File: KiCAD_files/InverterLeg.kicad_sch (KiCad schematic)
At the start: 94 parts, among them J801 Conn_Coaxial_Small, J802 Conn_Coaxial_Small, J804 Conn_01x03_Socket, J811 Screw_Terminal_01x01, J814 Screw_Terminal_01x01, J817 Screw_Terminal_01x01, J825 HC-PBB08-2-08-M-H4.0-G1-R-P-04, J827 HC-PBB08-2-08-M-H4.0-G1-R-P-04, J831 HC-PBB08-2-08-M-H4.0-G1-R-P-04, T801 TE1212-2W6ENT, T802 TE1212-2W6ENT, U603 UCC21520, U704 VPS8701B, U707 VPS8701B, U801 LT1761-SD, U802 LT1761-SD, U811 TMP117xxDRV, U815 TMP117xxDRV

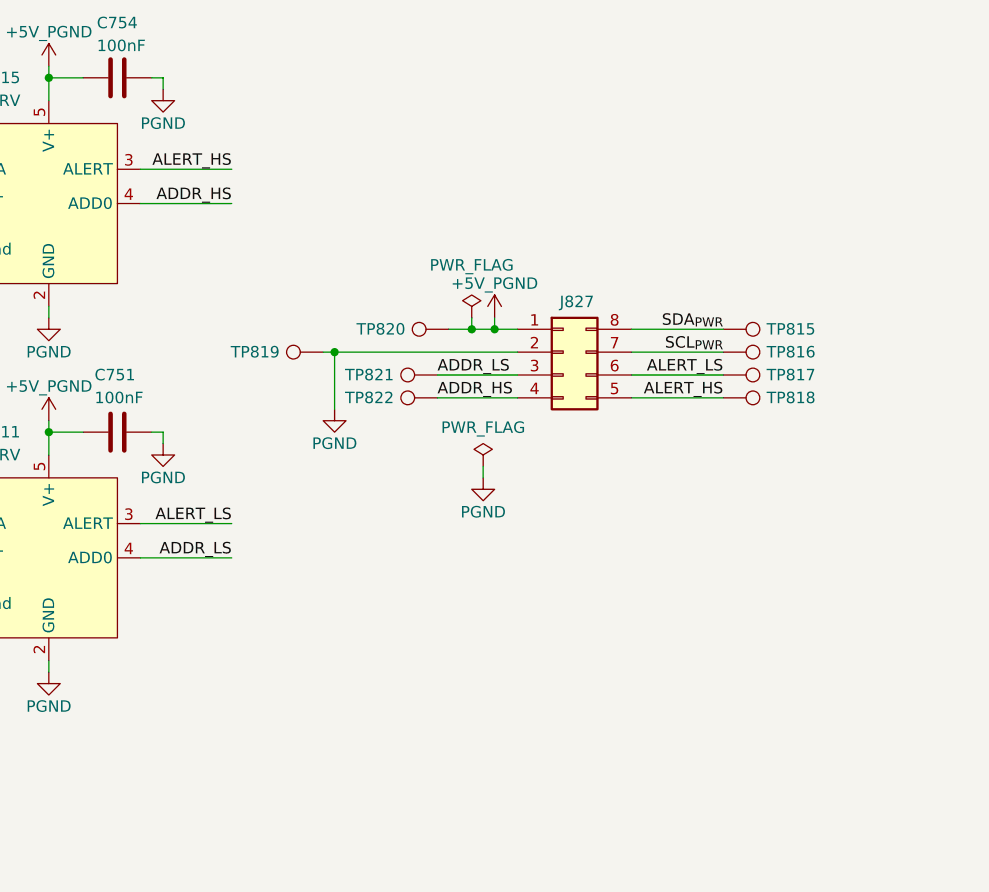
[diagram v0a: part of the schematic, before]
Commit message: Added an EEPROM footprint. Mooved slightly thermal sensor connector.
Signed-off-by: Jean Alinei <jean.alinei@owntech.org>
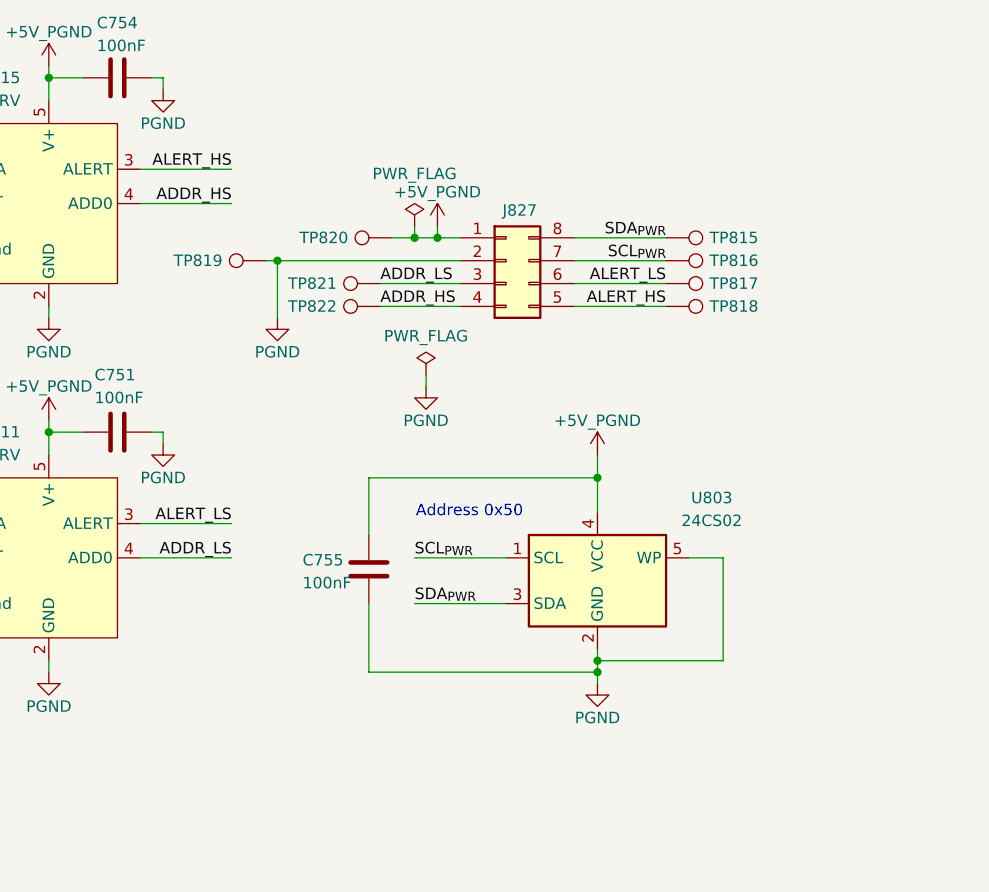
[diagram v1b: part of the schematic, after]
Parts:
- added C755: 100nF, Capacitor_SMD:C_0603_1608Metric, symbol Device:C
- added U803: 24CS02, Package_TO_SOT_SMD:SOT-23-5, symbol Symbols:24CS01
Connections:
- net +5V_PGND: now also C755.2, U803.4 (VCC)
- net PGND: now also C755.1, U803.2 (GND), U803.5 (WP)
- net SCL_{PWR}: now also U803.1 (SCL)
- net SDA_{PWR}: now also U803.3 (SDA)
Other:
- note added: "Address 0x50"
- moved on the sheet: J827, TP815, TP816, TP817, TP818, TP819, TP820, TP821, TP822

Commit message: Fixed LDO resistors values. Fixed capacitor values.
Signed-off-by: Jean Alinei <jean.alinei@owntech.org>
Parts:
- C602, C605, C612, C614: Reserved1 19d8e62435aae811d30466f8cc008899f37785f68fd5 -> (none)
- C604, C703: Reserved1 269e10abb8e08bedf6fe59138f738c816916bbb2d9 -> (none)
- C607, C608: value 100nF -> 1nF; LCSC C14663 -> C1588; Reserved1 19d8e62435aae811d30466f8cc008899f37785f68fd5 -> (none)
- C616: Reserved1 6ef4274804797e6557917bb79bd82a607ad050021f56b2 -> (none)
- C624, C626: Reserved1 0db098cf967df37918c59b0e08ade59c874a0accb68a991e -> (none)
- C709, C711, C717, C718, C719, C731, C732, C734: Reserved1 3c8c36ffa6a0eb88db22fa786b0d8984706c66e773e3ba -> (none)
- C713, C733, C751, C754, C755: Reserved1 2a7756d0bc30aa9cc4f0a80c55ca60c5e6f002aa0dc4 -> (none)
- R601, R603: Reserved1 e83d0d2e640bd473b48d7e0284fc3bc7586bd6985cc2 -> (none)
- R602, R604: Reserved1 b7f0312652245873b572e2e89e4b51494f4dce2bf518 -> (none)
- R605, R606: Reserved1 09f3912dc83c8a80315b578c251a24aaa57a6fa6cfa9 -> (none)
- R607, R608: Reserved1 587483f3fd3ad8d455ca46df31bb2751f8d4cf649ee8 -> (none)
- R610: value 178k -> 510k; Reserved1 09f3912dc83c8a80315b578c251a24aaa57a6fa6cfa9 -> (none)
- R611, R613: value 20k -> 27k
- R612: value 178k -> 510k
- U811, U815: value TMP117xxDRV -> TMP117B
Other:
- note added: "V_{OUT} = 0.6 x (1 + (R612/R613)) V_{OUT} = @{round(0.6*(1+510000/27000),2)}V"
- note removed: "V_{OUT} = VADJ (1 + (R612/R613)) + (I_{ADJ} * R612) V_{ADJ} = 1.22V I_{ADJ} = 30nA at 25°C So: V_{OUT} = @{round((1.22*(1+(${/8d0c1d66-35ef-4a53-a28f-436a11b54f42/153ae966-be28-4ef2-b43e-ea2e9beaff1f:Value}/${/8d0c1d66-35ef-4a53-a28f-436a11b54f42/9b8227a6-f6d8-4461-b56f-2b44b0c1a3de:Value}))+(0.00000003*${/8d0c1d66-35ef-4a53-a28f-436a11b54f42/153ae966-be28-4ef2-b43e-ea2e9beaff1f:Value}))*100)/100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"

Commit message: Updated all components descriptions & values & datasheet names.
Signed-off-by: Jean Alinei <jean.alinei@owntech.org>
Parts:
- D601, D602, D703, D704, D709, D710: value PMEG4010 -> PMEG4010ESBYL
- J801, J802: value Conn_Coaxial_Small -> AIPEX-4
- J803, J806: value (none) -> 2LC000-739
- J811, J814, J817: value Screw_Terminal_01x01 -> SMTSO3050CTJ
- J825, J827, J831: value HC-PBB08-2-08-M-H4.0-G1-R-P-04 -> HC-PBB08-2-08-M-H1.0-G1-R-P-04
- Q801, Q802: value (none) -> AGM15T05LL
- R610, R612: value 510k -> 178k
- R611, R613: value 27k -> 20k
- T801, T802: value TE1212-2W6ENT -> TE1212-1W6ENT
- TJ801, TJ804: value (none) -> THJP1206AST1
- U603: value UCC21520 -> UCC21520DWR
- U801, U802: value LT1761-SD -> SY6345AAC
- U803: value 24CS02 -> 24C02S(XBLW)
- U811, U815: value TMP117B -> T117B

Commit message: Changed signal connectors to male parts. Updated the 3D models.
Signed-off-by: Jean Alinei <jean.alinei@owntech.org>
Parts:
- J825, J827, J831: footprint Footprints:HC-PBB02-2-08-M -> Footprints:HC-PBB02-2-08-Male
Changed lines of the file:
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@@
 			)
 		)
-		(property "Footprint" "Footprints:HC-PBB02-2-08-M"
+		(property "Footprint" "Footprints:HC-PBB02-2-08-Male"
 			(at 62.23 193.04 0)
 			(hide yes)
@@
 			)
 		)
-		(property "Footprint" "Footprints:HC-PBB02-2-08-M"
+		(property "Footprint" "Footprints:HC-PBB02-2-08-Male"
 			(at 50.8 48.26 0)
 			(hide yes)
@@
 			)
 		)
-		(property "Footprint" "Footprints:HC-PBB02-2-08-M"
+		(property "Footprint" "Footprints:HC-PBB02-2-08-Male"
 			(at 360.68 101.6 0)
 			(hide yes)

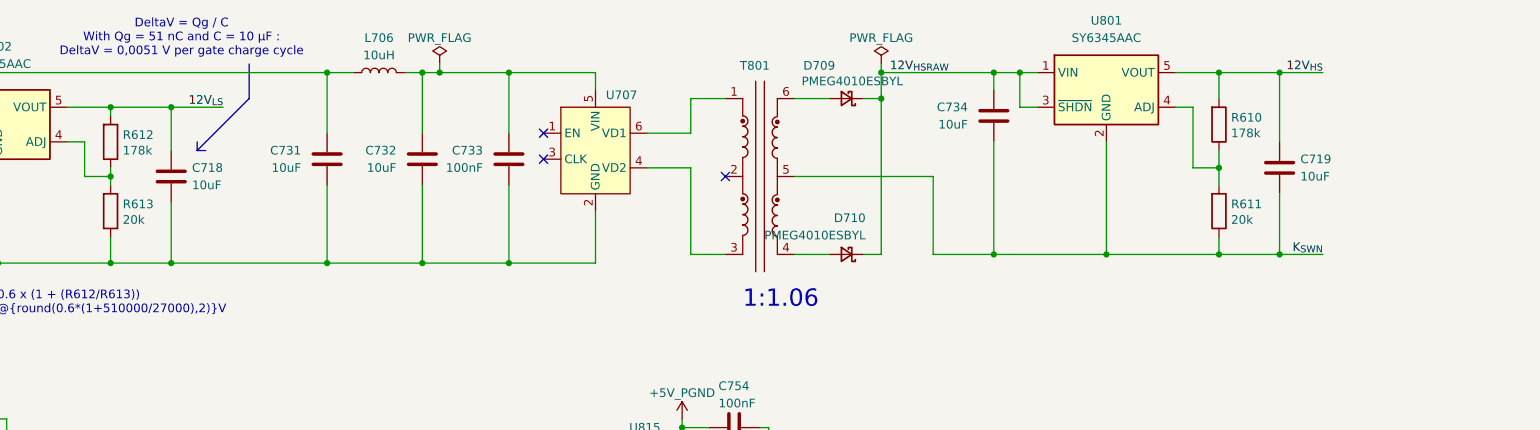
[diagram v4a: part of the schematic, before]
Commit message: Fixed ADJ resistors values.
Signed-off-by: Jean Alinei <jean.alinei@owntech.org>
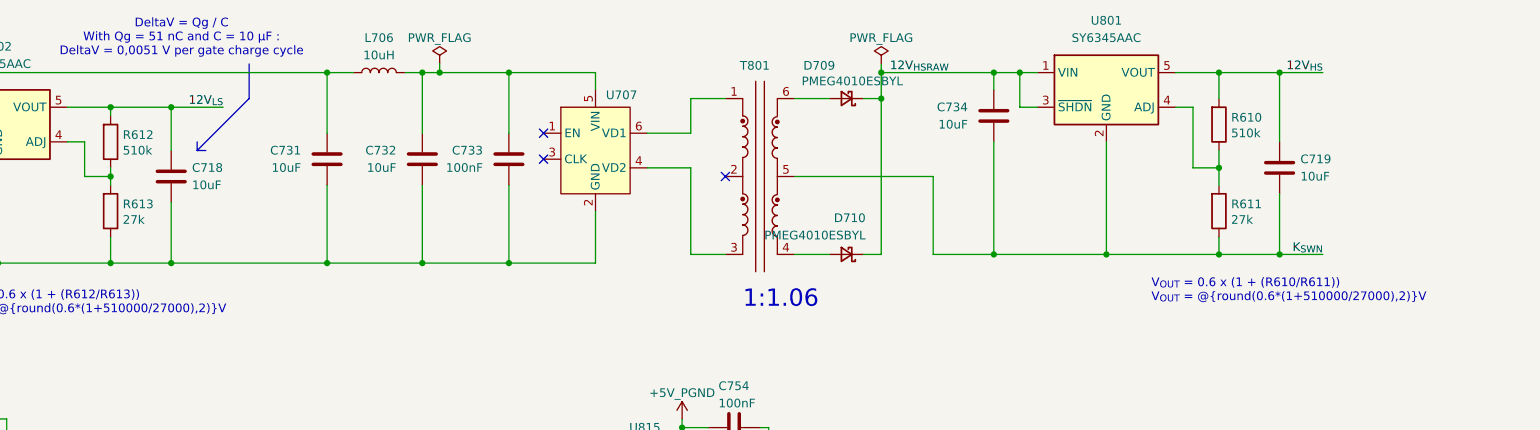
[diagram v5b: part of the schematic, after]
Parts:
- R610, R612: value 178k -> 510k; LCSC C26995 -> C11616
- R611, R613: value 20k -> 27k; LCSC C25765 -> C25771
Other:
- note added: "V_{OUT} = 0.6 x (1 + (R610/R611)) V_{OUT} = @{round(0.6*(1+510000/27000),2)}V"
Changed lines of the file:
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@@
 		)
 	)
+	(text "V_{OUT} = 0.6 x (1 + (R610/R611))\nV_{OUT} = @{round(0.6*(1+510000/27000),2)}V\n"
+		(exclude_from_sim no)
+		(at 378.714 61.214 0)
+		(effects
+			(font
+				(size 1.27 1.27)
+			)
+			(justify left)
+		)
+	)
 	(text "J831"
 		(exclude_from_sim no)
@@
 			)
 		)
-		(property "Value" "178k"
+		(property "Value" "510k"
 			(at 227.838 40.64 0)
 			(show_name no)
@@
 			)
 		)
-		(property "Description" "178 kohm +/-1%, 62.5 mW thick-film resistor, 0402; UNI-ROYAL 0402WGF1783TCE"
+		(property "Description" "510 kohm +/-1%, 62.5 mW thick-film resistor, 0402; UNI-ROYAL 0402WGF1783TCE"
 			(at 226.06 39.37 0)
 			(hide yes)
@@
 			)
 		)
-		(property "LCSC" "C26995"
+		(property "LCSC" "C11616"
 			(at 226.06 39.37 0)
 			(hide yes)
@@
 			)
 		)
-		(property "Value" "178k"
+		(property "Value" "510k"
 			(at 390.398 38.1 0)
 			(show_name no)
@@
 			)
 		)
-		(property "Description" "178 kohm +/-1%, 62.5 mW thick-film resistor, 0402; UNI-ROYAL 0402WGF1783TCE"
+		(property "Description" "510 kohm +/-1%, 62.5 mW thick-film resistor, 0402; UNI-ROYAL 0402WGF1783TCE"
 			(at 388.62 36.83 0)
 			(hide yes)
@@
 			)
 		)
-		(property "LCSC" "C26995"
+		(property "LCSC" "C11616"
 			(at 388.62 36.83 0)
 			(hide yes)
@@
 			)
 		)
-		(property "Value" "20k"
+		(property "Value" "27k"
 			(at 227.838 50.8 0)
 			(show_name no)
@@
 			)
 		)
-		(property "Description" "20 kohm +/-1%, 62.5 mW thick-film resistor, 0402; UNI-ROYAL 0402WGF2002TCE"
+		(property "Description" "27 kohm +/-1%, 62.5 mW thick-film resistor, 0402; UNI-ROYAL 0402WGF2002TCE"
 			(at 226.06 49.53 0)
 			(hide yes)
@@
 			)
 		)
-		(property "LCSC" "C25765"
+		(property "LCSC" "C25771"
 			(at 226.06 49.53 0)
 			(hide yes)
@@
 			)
 		)
-		(property "Value" "20k"
+		(property "Value" "27k"
 			(at 390.398 50.8 0)
 			(show_name no)
@@
 			)
 		)
-		(property "Description" "20 kohm +/-1%, 62.5 mW thick-film resistor, 0402; UNI-ROYAL 0402WGF2002TCE"
+		(property "Description" "27 kohm +/-1%, 62.5 mW thick-film resistor, 0402; UNI-ROYAL 0402WGF2002TCE"
 			(at 388.62 49.53 0)
 			(hide yes)
@@
 			)
 		)
-		(property "LCSC" "C25765"
+		(property "LCSC" "C25771"
 			(at 388.62 49.53 0)
 			(hide yes)

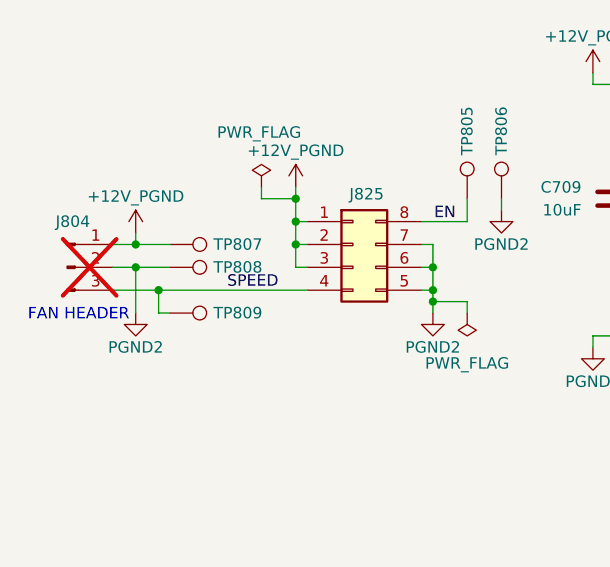
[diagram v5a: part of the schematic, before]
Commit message: Added FAN_ON pins.
Signed-off-by: Jean Alinei <jean.alinei@owntech.org>
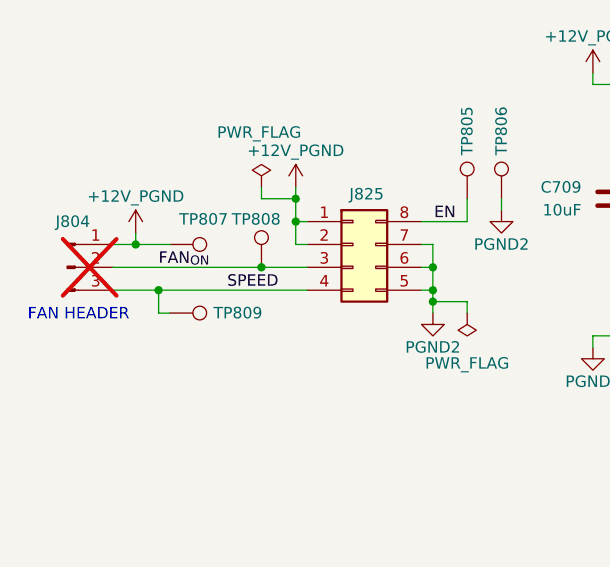
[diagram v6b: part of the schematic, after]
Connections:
- net +12V_PGND: no longer J825.3 (Pin_3)
- net PGND2: no longer J804.2 (Pin_2), TP808.1
- new net FAN_{ON}: J804.2 (Pin_2), J825.3 (Pin_3), TP808.1
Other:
- moved on the sheet: TP808
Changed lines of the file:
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@@
 	)
 	(junction
-		(at 26.67 50.8)
-		(diameter 0)
-		(color 0 0 0 0)
-	)
-	(junction
 		(at 59.69 50.8)
 		(diameter 0)
@@
 	)
 	(junction
-		(at 44.45 48.26)
-		(diameter 0)
-		(color 0 0 0 0)
-	)
-	(junction
 		(at 355.6 55.88)
 		(diameter 0)
@@
 	)
 	(junction
+		(at 40.64 50.8)
+		(diameter 0)
+		(color 0 0 0 0)
+	)
+	(junction
 		(at 194.31 104.14)
 		(diameter 0)
@@
 	(wire
 		(pts
-			(xy 24.13 50.8) (xy 26.67 50.8)
-		)
-		(stroke
-			(width 0)
-			(type default)
-		)
-	)
-	(wire
-		(pts
 			(xy 138.43 195.58) (xy 138.43 201.93)
 		)
@@
 	(wire
 		(pts
-			(xy 44.45 48.26) (xy 44.45 50.8)
-		)
-		(stroke
-			(width 0)
-			(type default)
-		)
-	)
-	(wire
-		(pts
 			(xy 285.75 139.7) (xy 298.45 139.7)
 		)
@@
 	(wire
 		(pts
+			(xy 40.64 50.8) (xy 45.72 50.8)
+		)
+		(stroke
+			(width 0)
+			(type default)
+		)
+	)
+	(wire
+		(pts
 			(xy 368.3 106.68) (xy 378.46 106.68)
 		)
@@
 	(wire
 		(pts
-			(xy 26.67 50.8) (xy 26.67 55.88)
-		)
-		(stroke
-			(width 0)
-			(type default)
-		)
-	)
-	(wire
-		(pts
 			(xy 77.47 30.48) (xy 80.01 30.48)
 		)
@@
 	(wire
 		(pts
-			(xy 30.48 50.8) (xy 26.67 50.8)
+			(xy 24.13 50.8) (xy 40.64 50.8)
 		)
 		(stroke
@@
 	(wire
 		(pts
-			(xy 44.45 50.8) (xy 45.72 50.8)
-		)
-		(stroke
-			(width 0)
-			(type default)
-		)
-	)
-	(wire
-		(pts
 			(xy 176.53 99.06) (xy 184.15 99.06)
 		)
@@
 		)
 	)
+	(label "FAN_{ON}"
+		(at 29.21 50.8 0)
+		(effects
+			(font
+				(size 1.27 1.27)
+			)
+			(justify left bottom)
+		)
+	)
 	(label "K_{SWN}"
 		(at 266.7 187.96 180)
@@
 	(symbol
 		(lib_id "Connector:TestPoint")
-		(at 30.48 50.8 270)
+		(at 40.64 50.8 0)
 		(unit 1)
 		(body_style 1)
@@
 		(dnp no)
 		(property "Reference" "TP808"
-			(at 35.306 50.8 90)
+			(at 37.338 45.466 0)
 			(show_name no)
 			(do_not_autoplace no)
@@
 		)
 		(property "Value" ""
-			(at 32.5121 53.34 0)
+			(at 43.18 48.7679 0)
 			(show_name no)
 			(do_not_autoplace no)
@@
 		)
 		(property "Footprint" "Footprints:TestPoint_Pad_D1.0mm_small_courtyard"
-			(at 30.48 55.88 0)
+			(at 45.72 50.8 0)
 			(hide yes)
 			(show_name no)
@@
 		)
 		(property "Datasheet" ""
-			(at 30.48 55.88 0)
+			(at 45.72 50.8 0)
 			(hide yes)
 			(show_name no)
@@
 		)
 		(property "Description" "test point"
-			(at 30.48 50.8 0)
+			(at 40.64 50.8 0)
 			(hide yes)
 			(show_name no)
@@
 		)
 		(property "Position Offset" ""
-			(at 30.48 50.8 90)
+			(at 40.64 50.8 90)
 			(hide yes)
 			(show_name no)
@@
 			)
 		)
-		(property "Datasheet" "${KIPRJMOD}\\datasheet\\cr-1858361.pdf"
+		(property "Datasheet" ""
 			(at 226.06 39.37 0)
 			(hide yes)
@@
 		(dnp no)
 		(property "Reference" "TP807"
-			(at 35.306 48.26 90)
+			(at 31.496 45.466 90)
 			(show_name no)
 			(do_not_autoplace no)
@@
 			)
 		)
-		(property "Datasheet" "${KIPRJMOD}\\datasheet\\cr-1858361.pdf"
+		(property "Datasheet" ""
 			(at 388.62 36.83 0)
 			(hide yes)
@@
 	)
 	(symbol
-		(lib_id "Symbols:PGND")
-		(at 26.67 55.88 0)
-		(unit 1)
-		(body_style 1)
-		(exclude_from_sim no)
-		(in_bom yes)
-		(on_board yes)
-		(in_pos_files yes)
-		(dnp no)
-		(property "Reference" "#PWR0820"
-			(at 26.67 62.23 0)
-			(hide yes)
-			(show_name no)
-			(do_not_autoplace no)
-			(effects
-				(font
-					(size 1.27 1.27)
-				)
-			)
-		)
-		(property "Value" "PGND2"
-			(at 26.67 59.69 0)
-			(show_name no)
-			(do_not_autoplace no)
-			(effects
-				(font
-					(size 1.27 1.27)
-				)
-			)
-		)
-		(property "Footprint" ""
-			(at 26.67 55.88 0)
-			(hide yes)
-			(show_name no)
-			(do_not_autoplace no)
-			(effects
-				(font
-					(size 1.27 1.27)
-				)
-			)
-		)
-		(property "Datasheet" ""
-			(at 26.67 55.88 0)
-			(hide yes)
-			(show_name no)
-			(do_not_autoplace no)
-			(effects
-				(font
-					(size 1.27 1.27)
-				)
-			)
-		)
-		(property "Description" "Power symbol creates a global label with name \"PGND\" , ground"
-			(at 26.67 55.88 0)
-			(hide yes)
-			(show_name no)
-			(do_not_autoplace no)
-			(effects
-				(font
-					(size 1.27 1.27)
-				)
-			)
-		)
-		(pin "1"
-		)
-		(instances
-			(project "InverterLeg"
-				(path "/8d0c1d66-35ef-4a53-a28f-436a11b54f42"
-					(reference "#PWR0820")
-					(unit 1)
-				)
-			)
-		)
-	)
-	(symbol
 		(lib_id "Device:C")
 		(at 107.95 43.18 0)
@@
 			)
 		)
-		(property "Datasheet" "${KIPRJMOD}\\datasheet\\cr-1858361.pdf"
+		(property "Datasheet" ""
 			(at 388.62 49.53 0)
 			(hide yes)
